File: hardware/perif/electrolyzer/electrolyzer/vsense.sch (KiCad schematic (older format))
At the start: 5 parts

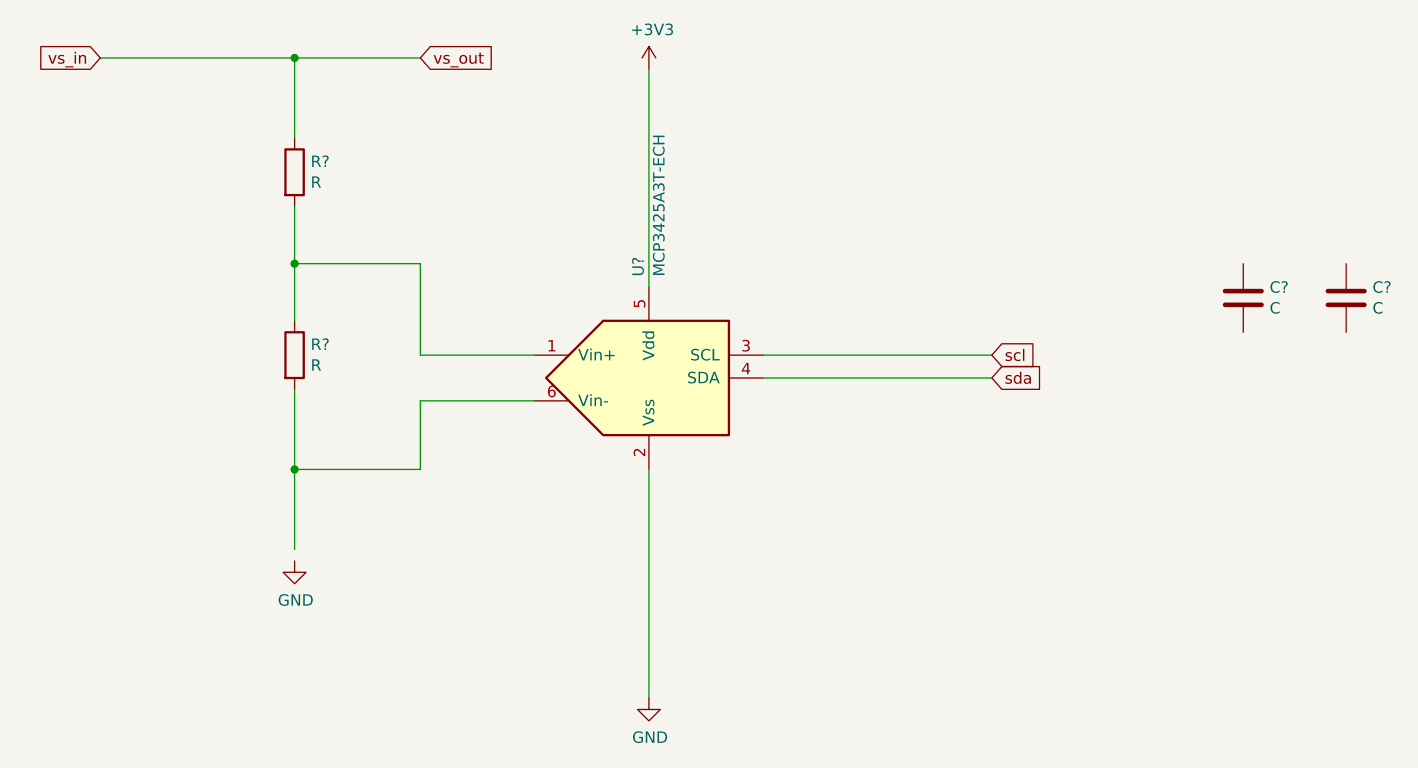
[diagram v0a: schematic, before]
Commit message: Started Electrolyzer board: sense
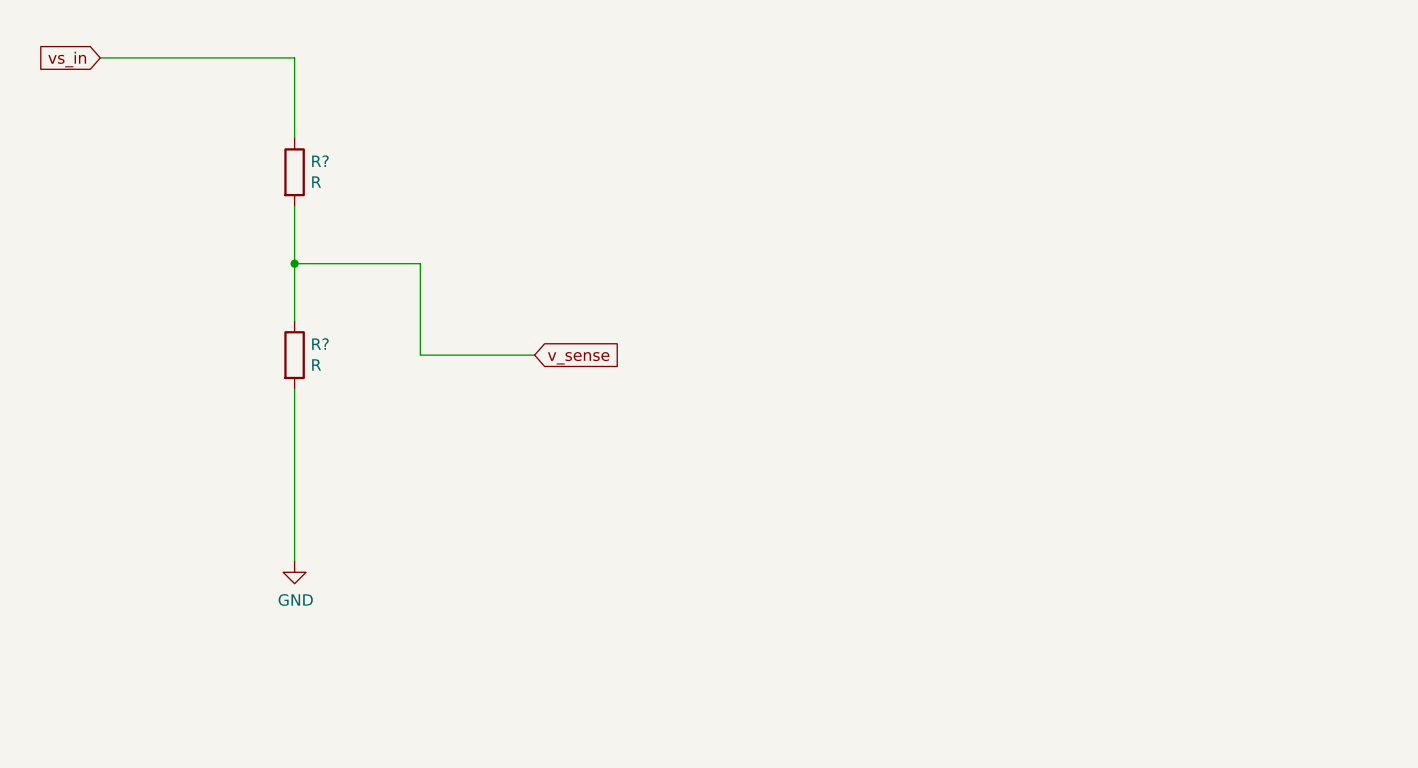
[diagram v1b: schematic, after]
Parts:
- removed C? (x2): C, symbol Device:C
- removed U?: MCP3425A3T-ECH, symbol Analog_ADC:MCP3425A3T-ECH
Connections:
- net labels added: v_sense
- net labels removed: +3V3, scl, sda, vs_out
- wire segments 17 -> 8
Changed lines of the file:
@@
 $EndDescr
-$Comp
-L Analog_ADC:MCP3425A3T-ECH U?
-U 1 1 5F1F8FE1
-P 3650 3900
-F 0 "U?" V 3604 4344 50  0000 L CNN
-F 1 "MCP3425A3T-ECH" V 3695 4344 50  0000 L CNN
-F 2 "" H 3650 3900 50  0001 C CIN
-F 3 "http://ww1.microchip.com/downloads/en/DeviceDoc/22072b.pdf" H 3650 3900 50  0001 C CNN
-	1    3650 3900
-	1    0    0    -1
-$EndComp
-$Comp
-L power:GND #PWR?
-U 1 1 5F1F8FE9
-P 3650 5300
-F 0 "#PWR?" H 3650 5050 50  0001 C CNN
-F 1 "GND" H 3655 5127 50  0000 C CNN
-F 2 "" H 3650 5300 50  0001 C CNN
-F 3 "" H 3650 5300 50  0001 C CNN
-	1    3650 5300
-	1    0    0    -1
-$EndComp
-$Comp
-L power:+3V3 #PWR?
-U 1 1 5F1F8FF1
-P 3650 2550
-F 0 "#PWR?" H 3650 2400 50  0001 C CNN
-F 1 "+3V3" H 3665 2723 50  0000 C CNN
-F 2 "" H 3650 2550 50  0001 C CNN
-F 3 "" H 3650 2550 50  0001 C CNN
-	1    3650 2550
-	1    0    0    -1
-$EndComp
-Text GLabel 5150 3800 2    50   Input ~ 0
-scl
-Text GLabel 5150 3900 2    50   Input ~ 0
-sda
-$Comp
-L Device:C C?
-U 1 1 5F1F8FFF
-P 6250 3550
-F 0 "C?" H 6365 3596 50  0000 L CNN
-F 1 "C" H 6365 3505 50  0000 L CNN
-F 2 "" H 6288 3400 50  0001 C CNN
-F 3 "~" H 6250 3550 50  0001 C CNN
-	1    6250 3550
-	1    0    0    -1
-$EndComp
-$Comp
-L Device:C C?
-U 1 1 5F1F9005
-P 6700 3550
-F 0 "C?" H 6815 3596 50  0000 L CNN
-F 1 "C" H 6815 3505 50  0000 L CNN
-F 2 "" H 6738 3400 50  0001 C CNN
-F 3 "~" H 6700 3550 50  0001 C CNN
-	1    6700 3550
-	1    0    0    -1
-$EndComp
-Wire Wire Line
-	3650 4300 3650 5300
-Wire Wire Line
-	3650 2550 3650 3500
-Wire Wire Line
-	4150 3900 5150 3900
-Wire Wire Line
-	4150 3800 5150 3800
 $Comp
 L Device:R R?
@@
 $EndComp
 Wire Wire Line
-	2100 4650 2100 4300
-Wire Wire Line
 	2100 3150 2100 3400
-Wire Wire Line
-	2650 4000 2650 4300
-Wire Wire Line
-	2650 4300 2100 4300
-Wire Wire Line
-	2650 4000 3150 4000
-Connection ~ 2100 4300
-Wire Wire Line
-	2100 4300 2100 3950
 Wire Wire Line
 	2100 3400 2650 3400
@@
 Text GLabel 1250 2500 0    50   Input ~ 0
 vs_in
-Text GLabel 2650 2500 2    50   Input ~ 0
-vs_out
 Wire Wire Line
 	1250 2500 2100 2500
 Wire Wire Line
 	2100 2850 2100 2500
-Connection ~ 2100 2500
+Text GLabel 3150 3800 2    50   Input ~ 0
+v_sense
 Wire Wire Line
-	2100 2500 2650 2500
+	2100 3950 2100 4700
 $EndSCHEMATC
